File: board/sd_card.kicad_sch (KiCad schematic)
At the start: 23 parts

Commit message: updated schematic
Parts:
- TP?: value TestPoint -> F5
- TP? (x2): value TestPoint -> F2
- TP?: value TestPoint -> F4; footprint (none) -> F3
- TP?: value TestPoint -> F1
- TP?: value TestPoint -> F6
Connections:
- net GND: now also U?.EP (GND)
- net ~{PowerOK}: now reaches C?.2, Q?.1 (G), Q?.3 (D), R?.1, R?.2
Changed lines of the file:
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@@
   (junction (at 173.99 80.01) (diameter 0) (color 0 0 0 0)
   )
+  (junction (at 226.06 62.23) (diameter 0) (color 0 0 0 0)
+  )
   (wire (pts (xy 87.63 88.9) (xy 88.9 88.9))
     (stroke (width 0) (type default) (color 0 0 0 0))
@@
     (stroke (width 0) (type default) (color 0 0 0 0))
   )
+  (wire (pts (xy 215.9 62.23) (xy 226.06 62.23))
+    (stroke (width 0) (type default) (color 0 0 0 0))
+  )
   (wire (pts (xy 154.94 88.9) (xy 154.94 73.66))
     (stroke (width 0) (type default) (color 0 0 0 0))
@@
     (stroke (width 0) (type default) (color 0 0 0 0))
   )
+  (wire (pts (xy 226.06 62.23) (xy 226.06 67.31))
+    (stroke (width 0) (type default) (color 0 0 0 0))
+  )
   (wire (pts (xy 167.64 62.23) (xy 179.07 62.23))
     (stroke (width 0) (type default) (color 0 0 0 0))
   )
-  (wire (pts (xy 226.06 54.61) (xy 226.06 67.31))
+  (wire (pts (xy 226.06 54.61) (xy 226.06 62.23))
     (stroke (width 0) (type default) (color 0 0 0 0))
   )
@@
   )
   (hierarchical_label "~{CS}" (shape input) (at 48.26 105.41 180)
+    (effects (font (size 1.27 1.27)) (justify right))
+  )
+  (hierarchical_label "~{PowerOK}" (shape output) (at 215.9 62.23 180)
     (effects (font (size 1.27 1.27)) (justify right))
   )
@@
       (effects (font (size 1.27 1.27)) (justify right))
     )
-    (property "Value" "TestPoint" (id 1) (at 87.63 148.0819 0)
+    (property "Value" "F5" (id 1) (at 87.63 148.0819 0)
       (effects (font (size 1.27 1.27)) (justify right))
     )
@@
       (effects (font (size 1.27 1.27)) (justify right))
     )
-    (property "Value" "TestPoint" (id 1) (at 92.71 135.3819 0)
+    (property "Value" "F2" (id 1) (at 92.71 135.3819 0)
       (effects (font (size 1.27 1.27)) (justify right))
     )
@@
       (effects (font (size 1.27 1.27)) (justify right))
     )
-    (property "Value" "TestPoint" (id 1) (at 90.17 141.7319 0)
-      (effects (font (size 1.27 1.27)) (justify right))
-    )
-    (property "Footprint" "" (id 2) (at 82.55 137.16 0)
+    (property "Value" "F4" (id 1) (at 90.17 141.7319 0)
+      (effects (font (size 1.27 1.27)) (justify right))
+    )
+    (property "Footprint" "F3" (id 2) (at 82.55 137.16 0)
       (effects (font (size 1.27 1.27)) hide)
     )
@@
       (effects (font (size 1.27 1.27)) (justify right))
     )
-    (property "Value" "TestPoint" (id 1) (at 97.79 122.6819 0)
+    (property "Value" "F1" (id 1) (at 97.79 122.6819 0)
       (effects (font (size 1.27 1.27)) (justify right))
     )
@@
       (effects (font (size 1.27 1.27)) (justify right))
     )
-    (property "Value" "TestPoint" (id 1) (at 95.25 129.0319 0)
+    (property "Value" "F2" (id 1) (at 95.25 129.0319 0)
       (effects (font (size 1.27 1.27)) (justify right))
     )
@@
     (pin "2")
   )
+  (symbol (lib_id "power:GND") (at 128.27 123.19 0) (unit 1)
+    (in_bom yes) (on_board yes) (fields_autoplaced)
+    (property "Reference" "#PWR?" (id 0) (at 128.27 129.54 0)
+      (effects (font (size 1.27 1.27)) hide)
+    )
+    (property "Value" "GND" (id 1) (at 128.27 128.27 0))
+    (property "Footprint" "" (id 2) (at 128.27 123.19 0)
+      (effects (font (size 1.27 1.27)) hide)
+    )
+    (property "Datasheet" "" (id 3) (at 128.27 123.19 0)
+      (effects (font (size 1.27 1.27)) hide)
+    )
+    (pin "1")
+  )
   (symbol (lib_id "power:+3V3") (at 226.06 40.64 0) (mirror y) (unit 1)
     (in_bom yes) (on_board yes) (fields_autoplaced)
@@
       (effects (font (size 1.27 1.27)) (justify right))
     )
-    (property "Value" "TestPoint" (id 1) (at 85.09 154.4319 0)
-      (effects (font (size 1.27 1.27)) (justify right))
-    )
+    (property "Value" "F6" (id 1) (at 85.09 154.4319 0)
+      (effects (font (size 1.27 1.27)) (justify right))
+    )

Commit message: updated schematic
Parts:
- FB?: value FerriteBead_Small -> BLM15BB
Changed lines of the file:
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@@
       (effects (font (size 1.27 1.27)) (justify left))
     )
-    (property "Value" "FerriteBead_Small" (id 1) (at 222.25 128.2318 0)
+    (property "Value" "BLM15BB" (id 1) (at 222.25 128.2318 0)
       (effects (font (size 1.27 1.27)) (justify left))
     )

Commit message: ERC run
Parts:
- gave numbers to parts that had none: 23

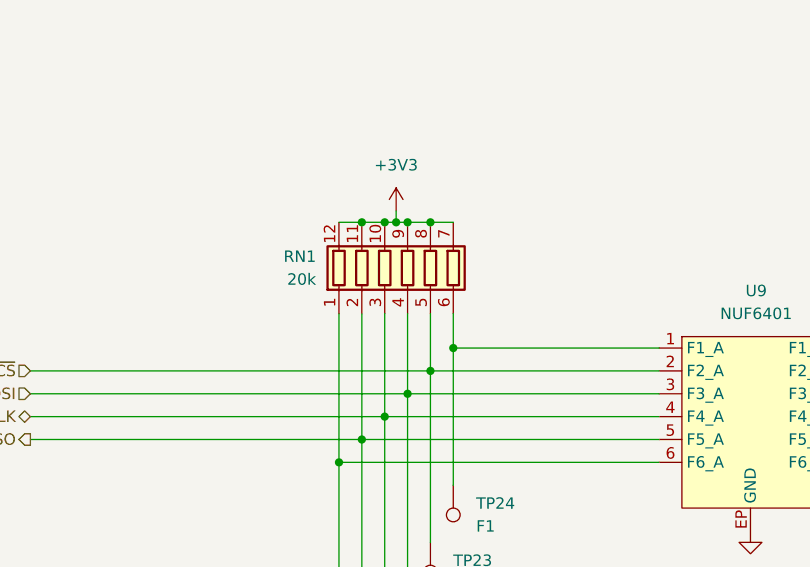
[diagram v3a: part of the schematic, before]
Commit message: added fuse and capacitor to schematic
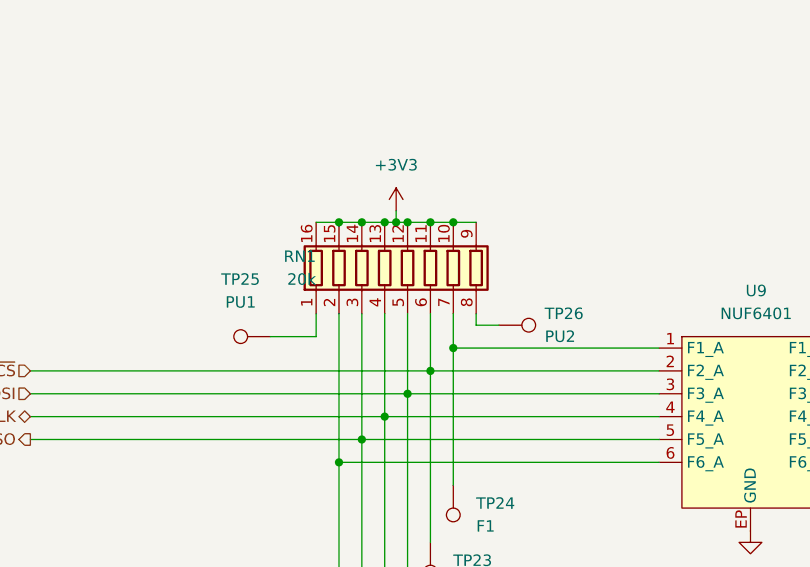
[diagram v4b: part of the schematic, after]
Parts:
- added TP25: PU1, symbol Connector:TestPoint
- added TP26: PU2, symbol Connector:TestPoint
- RN1: symbol Device:R_Pack06 -> Device:R_Pack08
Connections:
- net +3V3: now also RN1.13 (R4.2), RN1.14 (R3.2), RN1.15 (R2.2), RN1.16 (R1.2); no longer RN1.7 (R6.2), RN1.8 (R5.2)
- net CLK: now also RN1.4 (R4.1); no longer RN1.3 (R3.1)
- net MISO: now also RN1.3 (R3.1); no longer RN1.2 (R2.1)
- net MOSI: now also RN1.5 (R5.1); no longer RN1.4 (R4.1)
- net ~{CS}: now also RN1.6 (R6.1); no longer RN1.5 (R5.1)
- net at TP19.1, U9.6 (F6_A): now also RN1.2 (R2.1); no longer RN1.1 (R1.1)
- net at TP24.1, U9.1 (F1_A): now also RN1.7 (R7.1); no longer RN1.6 (R6.1)
- new net: RN1.1 (R1.1), TP25.1
- new net: RN1.8 (R8.1), TP26.1
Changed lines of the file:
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@@
   (junction (at 233.68 73.66) (diameter 0) (color 0 0 0 0)
   )
+  (junction (at 82.55 88.9) (diameter 0) (color 0 0 0 0)
+  )
   (junction (at 226.06 41.91) (diameter 0) (color 0 0 0 0)
   )
@@
   (junction (at 154.94 73.66) (diameter 0) (color 0 0 0 0)
   )
+  (junction (at 95.25 88.9) (diameter 0) (color 0 0 0 0)
+  )
   (junction (at 95.25 102.87) (diameter 0) (color 0 0 0 0)
   )
@@
     (stroke (width 0) (type default) (color 0 0 0 0))
   )
+  (wire (pts (xy 74.93 101.6) (xy 80.01 101.6))
+    (stroke (width 0) (type default) (color 0 0 0 0))
+  )
   (wire (pts (xy 170.18 113.03) (xy 171.45 113.03))
     (stroke (width 0) (type default) (color 0 0 0 0))
@@
     (stroke (width 0) (type default) (color 0 0 0 0))
   )
+  (wire (pts (xy 95.25 88.9) (xy 97.79 88.9))
+    (stroke (width 0) (type default) (color 0 0 0 0))
+  )
   (wire (pts (xy 156.21 102.87) (xy 139.7 102.87))
     (stroke (width 0) (type default) (color 0 0 0 0))
@@
     (stroke (width 0) (type default) (color 0 0 0 0))
   )
+  (wire (pts (xy 80.01 88.9) (xy 82.55 88.9))
+    (stroke (width 0) (type default) (color 0 0 0 0))
+  )
   (wire (pts (xy 92.71 99.06) (xy 92.71 105.41))
     (stroke (width 0) (type default) (color 0 0 0 0))
@@
     (stroke (width 0) (type default) (color 0 0 0 0))
   )
+  (wire (pts (xy 100.33 100.33) (xy 97.79 100.33))
+    (stroke (width 0) (type default) (color 0 0 0 0))
+  )
   (wire (pts (xy 179.07 54.61) (xy 179.07 53.34))
     (stroke (width 0) (type default) (color 0 0 0 0))
   )
+  (wire (pts (xy 97.79 100.33) (xy 97.79 99.06))
+    (stroke (width 0) (type default) (color 0 0 0 0))
+  )
   (wire (pts (xy 237.49 43.18) (xy 237.49 41.91))
     (stroke (width 0) (type default) (color 0 0 0 0))
@@
   )
   (wire (pts (xy 167.64 62.23) (xy 167.64 59.69))
+    (stroke (width 0) (type default) (color 0 0 0 0))
+  )
+  (wire (pts (xy 80.01 101.6) (xy 80.01 99.06))
     (stroke (width 0) (type default) (color 0 0 0 0))
   )
@@
     (pin "2")
   )
-  (symbol (lib_id "Device:R_Pack06") (at 90.17 93.98 0) (unit 1)
+  (symbol (lib_id "Device:R_Pack08") (at 90.17 93.98 0) (unit 1)
     (in_bom yes) (on_board yes) (fields_autoplaced)
     (property "Reference" "RN1" (id 0) (at 80.01 92.7099 0)
@@
       (effects (font (size 1.27 1.27)) (justify right))
     )
-    (property "Footprint" "" (id 2) (at 99.695 93.98 90)
+    (property "Footprint" "" (id 2) (at 102.235 93.98 90)
       (effects (font (size 1.27 1.27)) hide)
     )
@@
     (pin "11")
     (pin "12")
+    (pin "13")
+    (pin "14")
+    (pin "15")
+    (pin "16")
     (pin "2")
     (pin "3")
@@
     (pin "8")
     (pin "9")
+  )
+  (symbol (lib_id "Connector:TestPoint") (at 100.33 100.33 270) (unit 1)
+    (in_bom yes) (on_board yes) (fields_autoplaced)
+    (property "Reference" "TP26" (id 0) (at 105.41 99.0599 90)
+      (effects (font (size 1.27 1.27)) (justify left))
+    )
+    (property "Value" "PU2" (id 1) (at 105.41 101.5999 90)
+      (effects (font (size 1.27 1.27)) (justify left))
+    )
+    (property "Footprint" "" (id 2) (at 100.33 105.41 0)
+      (effects (font (size 1.27 1.27)) hide)
+    )
+    (property "Datasheet" "~" (id 3) (at 100.33 105.41 0)
+      (effects (font (size 1.27 1.27)) hide)
+    )
+    (pin "1")
   )
   (symbol (lib_id "Device:R_Small") (at 237.49 45.72 180) (unit 1)
@@
     (pin "2")
   )
+  (symbol (lib_id "Connector:TestPoint") (at 74.93 101.6 90) (unit 1)
+    (in_bom yes) (on_board yes) (fields_autoplaced)
+    (property "Reference" "TP25" (id 0) (at 71.628 95.25 90))
+    (property "Value" "PU1" (id 1) (at 71.628 97.79 90))
+    (property "Footprint" "" (id 2) (at 74.93 96.52 0)
+      (effects (font (size 1.27 1.27)) hide)
+    )
+    (property "Datasheet" "~" (id 3) (at 74.93 96.52 0)
+      (effects (font (size 1.27 1.27)) hide)
+    )
+    (pin "1")
+  )
   (symbol (lib_id "power:PWR_FLAG") (at 151.13 73.66 90) (unit 1)

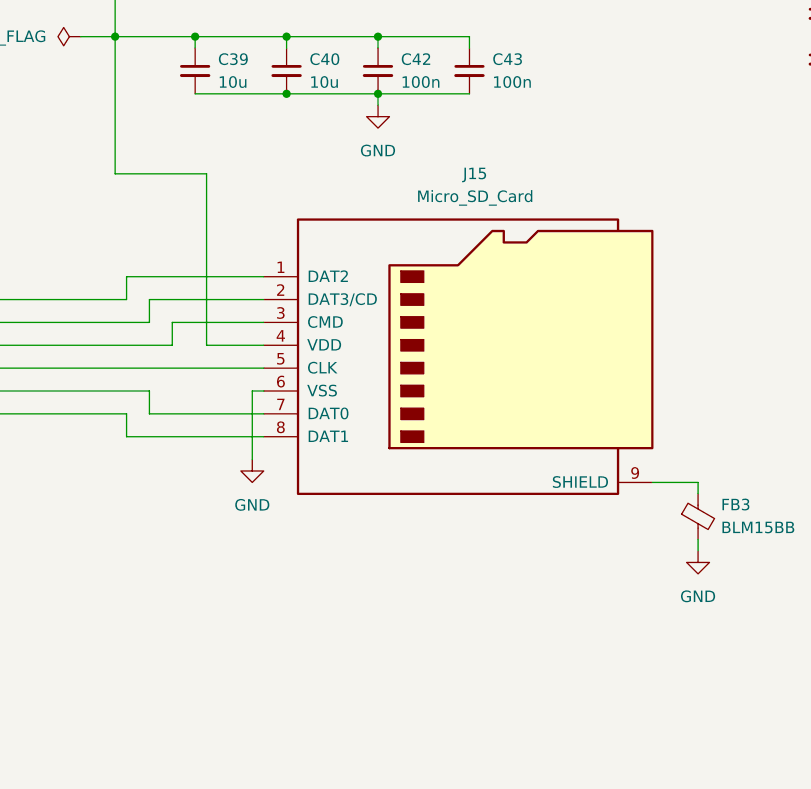
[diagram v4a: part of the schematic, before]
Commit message: added footprints to symbols and started layout
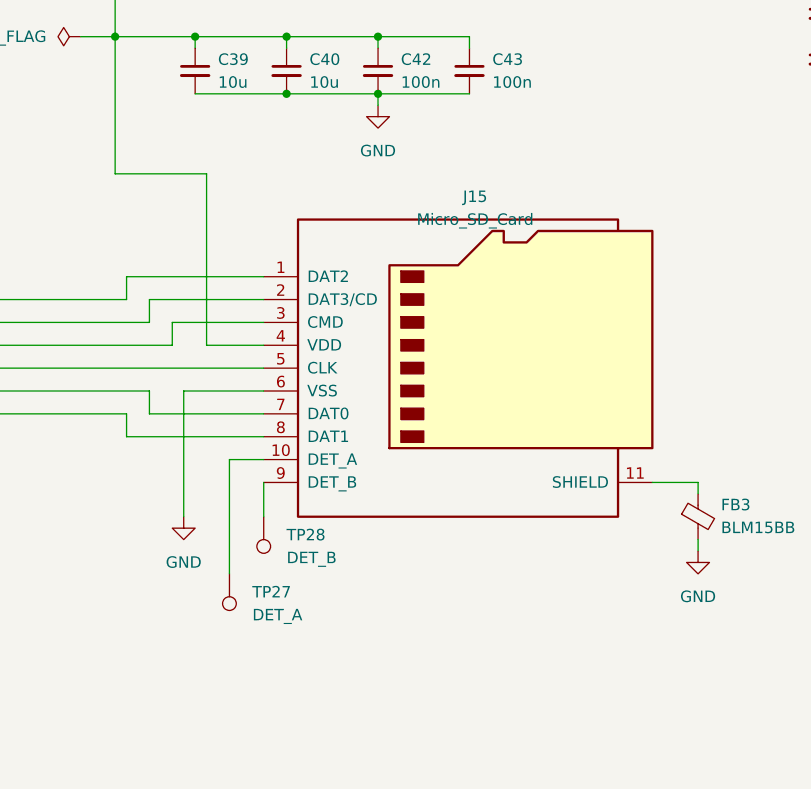
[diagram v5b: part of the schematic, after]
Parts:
- added TP27: DET_A, TestPoint:TestPoint_Pad_D1.0mm, symbol Connector:TestPoint
- added TP28: DET_B, TestPoint:TestPoint_Pad_D1.0mm, symbol Connector:TestPoint
- C39, C40, C41: footprint (none) -> Capacitor_SMD:C_0603_1608Metric
- C42, C43, C44, C45, FB3: footprint (none) -> Capacitor_SMD:C_0402_1005Metric
- J15: footprint (none) -> ownLib:GCT MEM2061; symbol Connector:Micro_SD_Card -> Connector:Micro_SD_Card_Det
- R24, R25, R26: footprint (none) -> Resistor_SMD:R_0402_1005Metric
- RN1: footprint (none) -> Resistor_SMD:R_Array_Convex_8x0602
- TP19, TP20, TP22, TP23, TP24, TP25, TP26: footprint (none) -> TestPoint:TestPoint_Pad_D1.0mm
- TP21: footprint F3 -> TestPoint:TestPoint_Pad_D1.0mm
- U10: footprint (none) -> Package_TO_SOT_SMD:SOT-23-5
- U9: footprint (none) -> ownLib:NUF6401
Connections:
- net at FB3.1: now also J15.11 (SHIELD); no longer J15.9 (SHIELD)
- new net: J15.10 (DET_A), TP27.1
- new net: J15.9 (DET_B), TP28.1

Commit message: finished layout for review
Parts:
- removed TP27: DET_A, TestPoint:TestPoint_Pad_D1.0mm, symbol Connector:TestPoint
- removed TP28: DET_B, TestPoint:TestPoint_Pad_D1.0mm, symbol Connector:TestPoint
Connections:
- net +3V3: now also J15.10 (DET_A)
- net CardDet: now reaches J15.9 (DET_B)
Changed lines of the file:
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@@
-    (stroke (width 0) (type default) (color 0 0 0 0))
-  )
-  (wire (pts (xy 167.64 120.65) (xy 167.64 133.35))
     (stroke (width 0) (type default) (color 0 0 0 0))
   )
@@
     (stroke (width 0) (type default) (color 0 0 0 0))
   )
-  (wire (pts (xy 171.45 120.65) (xy 167.64 120.65))
+  (wire (pts (xy 166.37 120.65) (xy 171.45 120.65))
     (stroke (width 0) (type default) (color 0 0 0 0))
   )
@@
   )
   (wire (pts (xy 139.7 115.57) (xy 156.21 115.57))
+    (stroke (width 0) (type default) (color 0 0 0 0))
+  )
+  (wire (pts (xy 166.37 120.65) (xy 166.37 135.89))
     (stroke (width 0) (type default) (color 0 0 0 0))
   )
@@
   )
   (hierarchical_label "~{CS}" (shape input) (at 48.26 105.41 180)
+    (effects (font (size 1.27 1.27)) (justify right))
+  )
+  (hierarchical_label "CardDet" (shape output) (at 171.45 127 270)
     (effects (font (size 1.27 1.27)) (justify right))
   )
@@
     (pin "9")
   )
+  (symbol (lib_id "power:+3V3") (at 166.37 135.89 180) (unit 1)
+    (in_bom yes) (on_board yes) (fields_autoplaced)
+    (property "Reference" "#PWR0102" (id 0) (at 166.37 132.08 0)
+      (effects (font (size 1.27 1.27)) hide)
+    )
+    (property "Value" "+3V3" (id 1) (at 168.91 137.1599 0)
+      (effects (font (size 1.27 1.27)) (justify right))
+    )
+    (property "Footprint" "" (id 2) (at 166.37 135.89 0)
+      (effects (font (size 1.27 1.27)) hide)
+    )
+    (property "Datasheet" "" (id 3) (at 166.37 135.89 0)
+      (effects (font (size 1.27 1.27)) hide)
+    )
+    (pin "1")
+  )
   (symbol (lib_id "Connector:TestPoint") (at 100.33 100.33 270) (unit 1)
     (in_bom yes) (on_board yes) (fields_autoplaced)
@@
     (pin "2")
     (pin "3")
-  )
-  (symbol (lib_id "Connector:TestPoint") (at 171.45 127 180) (unit 1)
-    (in_bom yes) (on_board yes) (fields_autoplaced)
-    (property "Reference" "TP28" (id 0) (at 173.99 129.0319 0)
-      (effects (font (size 1.27 1.27)) (justify right))
-    )
-    (property "Value" "DET_B" (id 1) (at 173.99 131.5719 0)
-      (effects (font (size 1.27 1.27)) (justify right))
-    )
-    (property "Footprint" "TestPoint:TestPoint_Pad_D1.0mm" (id 2) (at 166.37 127 0)
-      (effects (font (size 1.27 1.27)) hide)
-    )
-    (property "Datasheet" "~" (id 3) (at 166.37 127 0)
-      (effects (font (size 1.27 1.27)) hide)
-    )
-    (pin "1")
   )
   (symbol (lib_id "ownLib:NUF6401") (at 129.54 109.22 0) (unit 1)
@@
       (effects (font (size 1.27 1.27)) hide)
     )
-    (pin "1")
-  )
-  (symbol (lib_id "Connector:TestPoint") (at 167.64 133.35 180) (unit 1)
-    (in_bom yes) (on_board yes) (fields_autoplaced)
-    (property "Reference" "TP27" (id 0) (at 170.18 135.3819 0)
-      (effects (font (size 1.27 1.27)) (justify right))
-    )
-    (property "Value" "DET_A" (id 1) (at 170.18 137.9219 0)
-      (effects (font (size 1.27 1.27)) (justify right))
-    )
-    (property "Footprint" "TestPoint:TestPoint_Pad_D1.0mm" (id 2) (at 162.56 133.35 0)
-      (effects (font (size 1.27 1.27)) hide)
-    )
-    (property "Datasheet" "~" (id 3) (at 162.56 133.35 0)
-      (effects (font (size 1.27 1.27)) hide)
-    )

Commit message: worked feedback into layout
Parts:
- added R29: 100k, Resistor_SMD:R_0402_1005Metric, symbol Device:R_Small
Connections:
- net CardDet: now also R29.1
- net GND: now also R29.2
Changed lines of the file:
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@@
   (junction (at 167.64 53.34) (diameter 0) (color 0 0 0 0)
   )
+  (junction (at 171.45 132.08) (diameter 0) (color 0 0 0 0)
+  )
   (junction (at 163.83 73.66) (diameter 0) (color 0 0 0 0)
   )
@@
     (stroke (width 0) (type default) (color 0 0 0 0))
   )
+  (wire (pts (xy 179.07 132.08) (xy 171.45 132.08))
+    (stroke (width 0) (type default) (color 0 0 0 0))
+  )
   (wire (pts (xy 162.56 113.03) (xy 171.45 113.03))
     (stroke (width 0) (type default) (color 0 0 0 0))
@@
     (stroke (width 0) (type default) (color 0 0 0 0))
   )
-  (wire (pts (xy 171.45 123.19) (xy 171.45 127))
+  (wire (pts (xy 171.45 123.19) (xy 171.45 132.08))
     (stroke (width 0) (type default) (color 0 0 0 0))
   )
@@
     (stroke (width 0) (type default) (color 0 0 0 0))
   )
+  (wire (pts (xy 179.07 139.7) (xy 179.07 140.97))
+    (stroke (width 0) (type default) (color 0 0 0 0))
+  )
   (wire (pts (xy 92.71 99.06) (xy 92.71 105.41))
     (stroke (width 0) (type default) (color 0 0 0 0))
@@
     (stroke (width 0) (type default) (color 0 0 0 0))
   )
+  (wire (pts (xy 171.45 132.08) (xy 171.45 147.32))
+    (stroke (width 0) (type default) (color 0 0 0 0))
+  )
   (wire (pts (xy 88.9 87.63) (xy 88.9 88.9))
     (stroke (width 0) (type default) (color 0 0 0 0))
@@
   )
   (wire (pts (xy 184.15 80.01) (xy 184.15 81.28))
+    (stroke (width 0) (type default) (color 0 0 0 0))
+  )
+  (wire (pts (xy 179.07 134.62) (xy 179.07 132.08))
     (stroke (width 0) (type default) (color 0 0 0 0))
   )
@@
     (effects (font (size 1.27 1.27)) (justify right))
   )
-  (hierarchical_label "CardDet" (shape output) (at 171.45 127 270)
+  (hierarchical_label "CardDet" (shape output) (at 171.45 147.32 270)
     (effects (font (size 1.27 1.27)) (justify right))
   )
@@
   )
   (symbol (lib_id "power:+3V3") (at 166.37 135.89 180) (unit 1)
-    (in_bom yes) (on_board yes) (fields_autoplaced)
+    (in_bom yes) (on_board yes)
     (property "Reference" "#PWR0102" (id 0) (at 166.37 132.08 0)
       (effects (font (size 1.27 1.27)) hide)
     )
-    (property "Value" "+3V3" (id 1) (at 168.91 137.1599 0)
+    (property "Value" "+3V3" (id 1) (at 166.37 144.78 90)
       (effects (font (size 1.27 1.27)) (justify right))
     )
@@
     (pin "2")
   )
+  (symbol (lib_id "power:GND") (at 179.07 140.97 0) (unit 1)
+    (in_bom yes) (on_board yes) (fields_autoplaced)
+    (property "Reference" "#PWR0103" (id 0) (at 179.07 147.32 0)
+      (effects (font (size 1.27 1.27)) hide)
+    )
+    (property "Value" "GND" (id 1) (at 179.07 146.05 0))
+    (property "Footprint" "" (id 2) (at 179.07 140.97 0)
+      (effects (font (size 1.27 1.27)) hide)
+    )
+    (property "Datasheet" "" (id 3) (at 179.07 140.97 0)
+      (effects (font (size 1.27 1.27)) hide)
+    )
+    (pin "1")
+  )
   (symbol (lib_id "Device:C_Small") (at 163.83 77.47 0) (unit 1)
     (in_bom yes) (on_board yes) (fields_autoplaced)
@@
     (pin "1")
   )
+  (symbol (lib_id "Device:R_Small") (at 179.07 137.16 0) (unit 1)
+    (in_bom yes) (on_board yes) (fields_autoplaced)
+    (property "Reference" "R29" (id 0) (at 181.61 135.8899 0)
+      (effects (font (size 1.27 1.27)) (justify left))
+    )
+    (property "Value" "100k" (id 1) (at 181.61 138.4299 0)
+      (effects (font (size 1.27 1.27)) (justify left))
+    )
+    (property "Footprint" "Resistor_SMD:R_0402_1005Metric" (id 2) (at 179.07 137.16 0)
+      (effects (font (size 1.27 1.27)) hide)
+    )
+    (property "Datasheet" "~" (id 3) (at 179.07 137.16 0)
+      (effects (font (size 1.27 1.27)) hide)
+    )
+    (pin "1")
+    (pin "2")
+  )
   (symbol (lib_id "Device:Q_PMOS_GSD") (at 157.48 62.23 180) (unit 1)

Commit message: did some minor stuff
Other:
- company: (none) -> Hochschule Pforzheim
- title: (none) -> eduSignal
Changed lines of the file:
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@@
 (kicad_sch (version 20211123) (generator eeschema)
   (paper "A4")
+  (title_block
+    (title "eduSignal")
+    (date "2022-07-14")
+    (rev "1")
+    (company "Hochschule Pforzheim")
+    (comment 1 "Patrick Hanner")
+    (comment 2 "Biosignal development board")
+  )
   (junction (at 90.17 88.9) (diameter 0) (color 0 0 0 0)
   )
